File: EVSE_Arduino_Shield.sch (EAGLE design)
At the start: 45 parts, among them IC1 TLV1805DBVR, IC2 MT3608, IC3 TC1044S_OA, U2 ARDUINOR3-DIMENSION

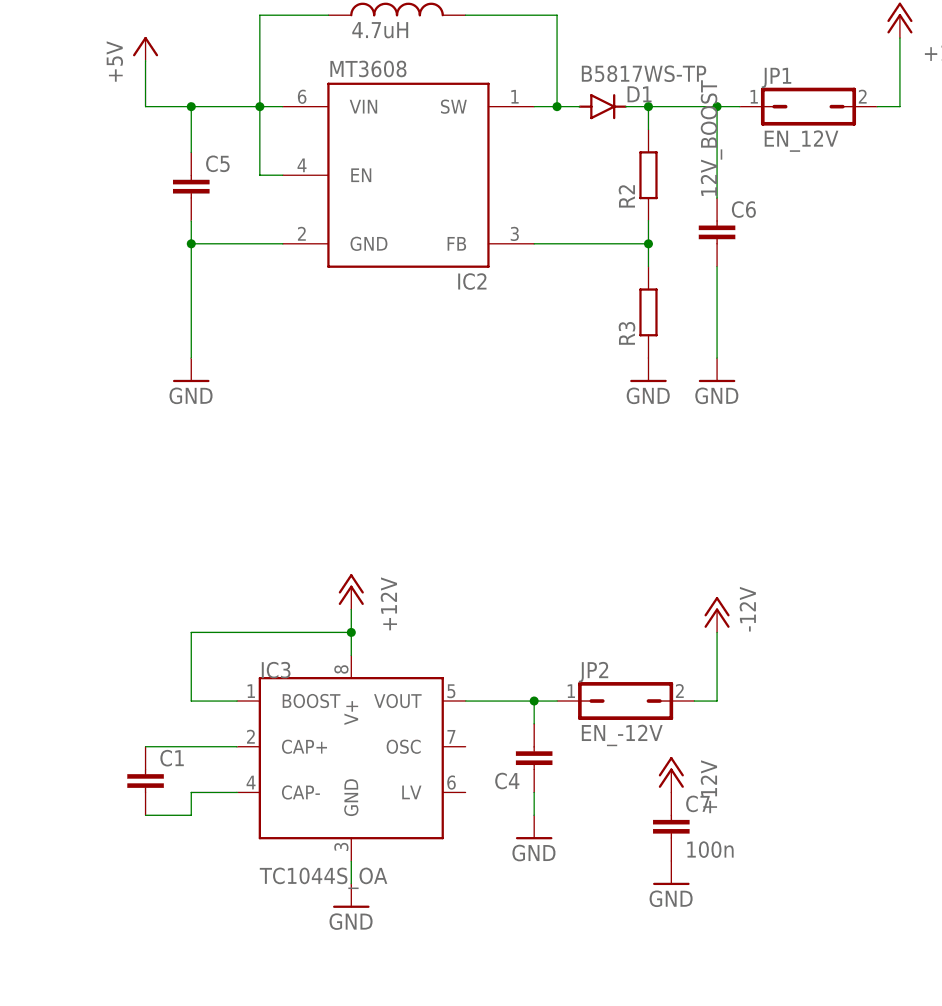
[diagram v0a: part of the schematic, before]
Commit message: * Fixed missing values of R2, R3, C5, C1, C6, C4
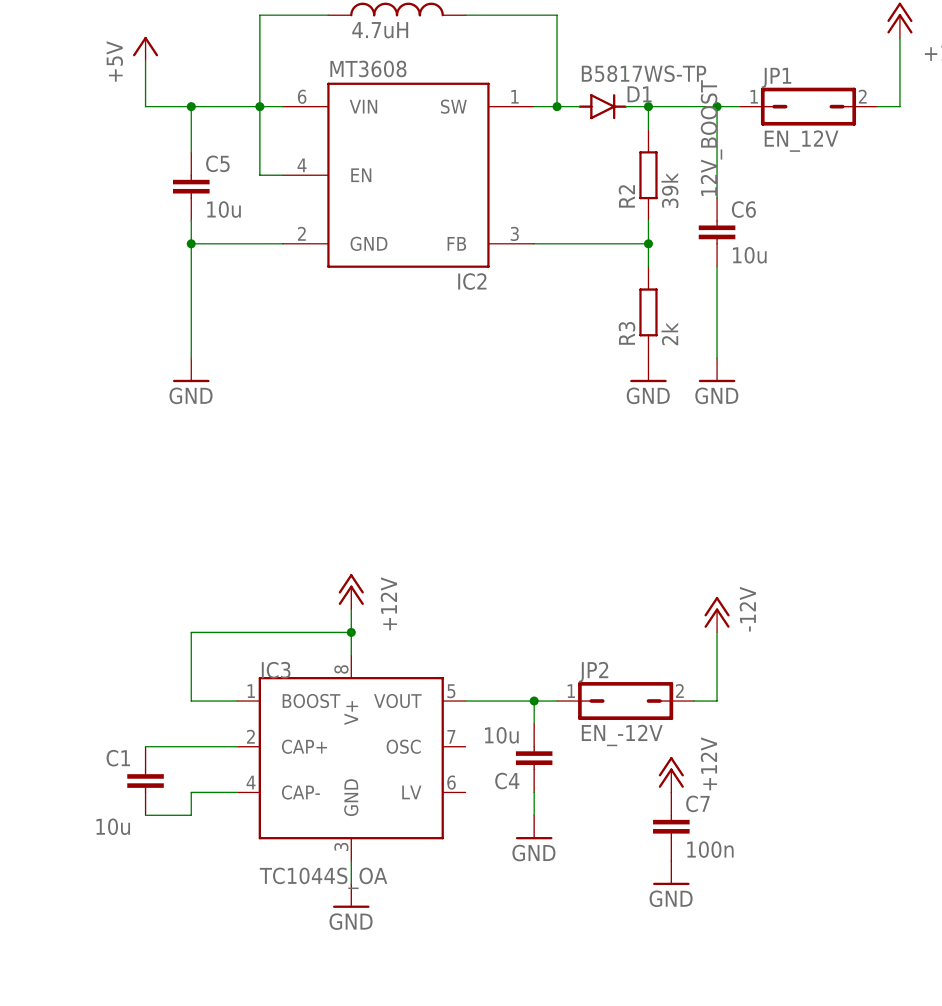
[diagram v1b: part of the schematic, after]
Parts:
- C1, C4, C5, C6: value (none) -> 10u
- R2: value (none) -> 39k
- R3: value (none) -> 2k
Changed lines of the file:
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@@
 <part name="GND6" library="supply1" library_urn="urn:adsk.eagle:library:371" deviceset="GND" device=""/>
 <part name="P-1" library="supply1" library_urn="urn:adsk.eagle:library:371" deviceset="-12V" device=""/>
-<part name="C1" library="rcl" library_urn="urn:adsk.eagle:library:334" deviceset="C-EU" device="C0805" package3d_urn="urn:adsk.eagle:package:23617/2"/>
-<part name="C4" library="rcl" library_urn="urn:adsk.eagle:library:334" deviceset="C-EU" device="C0805" package3d_urn="urn:adsk.eagle:package:23617/2"/>
+<part name="C1" library="rcl" library_urn="urn:adsk.eagle:library:334" deviceset="C-EU" device="C0805" package3d_urn="urn:adsk.eagle:package:23617/2" value="10u"/>
+<part name="C4" library="rcl" library_urn="urn:adsk.eagle:library:334" deviceset="C-EU" device="C0805" package3d_urn="urn:adsk.eagle:package:23617/2" value="10u"/>
 <part name="SV1" library="con-lstb" library_urn="urn:adsk.eagle:library:162" deviceset="MA03-1" device="" package3d_urn="urn:adsk.eagle:package:8339/1" value="12V_Test"/>
 <part name="GND1" library="supply1" library_urn="urn:adsk.eagle:library:371" deviceset="GND" device=""/>
@@
 <part name="IC2" library="Eigene-Rietig" library_urn="urn:adsk.eagle:library:40964436" deviceset="MT3608" device="" package3d_urn="urn:adsk.eagle:package:41021867/1"/>
 <part name="D1" library="diode" library_urn="urn:adsk.eagle:library:210" deviceset="DIODE-" device="SOD323-R" package3d_urn="urn:adsk.eagle:package:43437/1" value="B5817WS-TP"/>
-<part name="R2" library="rcl" library_urn="urn:adsk.eagle:library:334" deviceset="R-EU_" device="R0603" package3d_urn="urn:adsk.eagle:package:23555/3"/>
-<part name="R3" library="rcl" library_urn="urn:adsk.eagle:library:334" deviceset="R-EU_" device="R0603" package3d_urn="urn:adsk.eagle:package:23555/3"/>
-<part name="C5" library="rcl" library_urn="urn:adsk.eagle:library:334" deviceset="C-EU" device="C0805" package3d_urn="urn:adsk.eagle:package:23617/2"/>
-<part name="C6" library="rcl" library_urn="urn:adsk.eagle:library:334" deviceset="C-EU" device="C0805" package3d_urn="urn:adsk.eagle:package:23617/2"/>
+<part name="R2" library="rcl" library_urn="urn:adsk.eagle:library:334" deviceset="R-EU_" device="R0603" package3d_urn="urn:adsk.eagle:package:23555/3" value="39k"/>
+<part name="R3" library="rcl" library_urn="urn:adsk.eagle:library:334" deviceset="R-EU_" device="R0603" package3d_urn="urn:adsk.eagle:package:23555/3" value="2k"/>
+<part name="C5" library="rcl" library_urn="urn:adsk.eagle:library:334" deviceset="C-EU" device="C0805" package3d_urn="urn:adsk.eagle:package:23617/2" value="10u"/>
+<part name="C6" library="rcl" library_urn="urn:adsk.eagle:library:334" deviceset="C-EU" device="C0805" package3d_urn="urn:adsk.eagle:package:23617/2" value="10u"/>
 <part name="P+3" library="supply1" deviceset="+12V" device=""/>
 <part name="GND7" library="supply1" library_urn="urn:adsk.eagle:library:371" deviceset="GND" device=""/>
@@
 </instance>
 <instance part="C1" gate="G$1" x="30.48" y="137.16" smashed="yes">
-<attribute name="NAME" x="32.004" y="137.541" size="1.778" layer="95"/>
-<attribute name="VALUE" x="32.004" y="132.461" size="1.778" layer="96"/>
+<attribute name="NAME" x="28.956" y="139.319" size="1.778" layer="95" rot="R180"/>
+<attribute name="VALUE" x="28.956" y="131.699" size="1.778" layer="96" rot="R180"/>
 </instance>
 <instance part="C4" gate="G$1" x="73.66" y="137.16" smashed="yes" rot="R180">
@@
 </instance>
 <instance part="P+8" gate="1" x="88.9" y="137.16" smashed="yes">
-<attribute name="VALUE" x="93.98" y="132.08" size="1.778" layer="96" rot="R90"/>
+<attribute name="VALUE" x="93.98" y="134.62" size="1.778" layer="96" rot="R90"/>
 </instance>
 <instance part="C7" gate="G$1" x="88.9" y="132.08" smashed="yes">

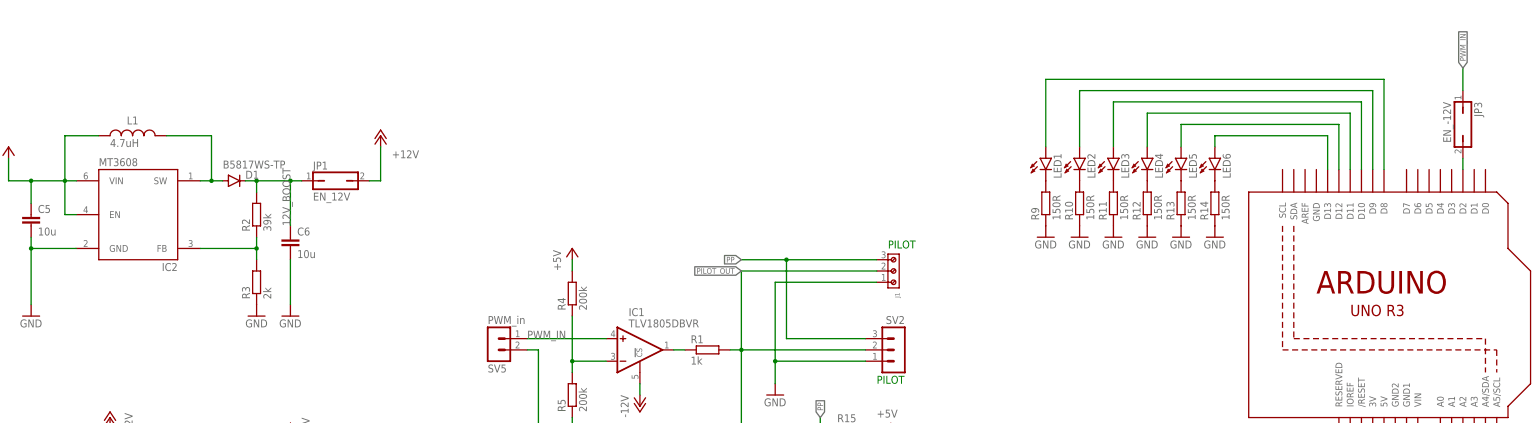
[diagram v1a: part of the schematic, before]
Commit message: * Cleaned Code a bit * Fixed Issue #1 - PWM is now on D3 * Fixed Issue #2 . MT3608 has the correct pin out now * Re-generated GERBER and SCH
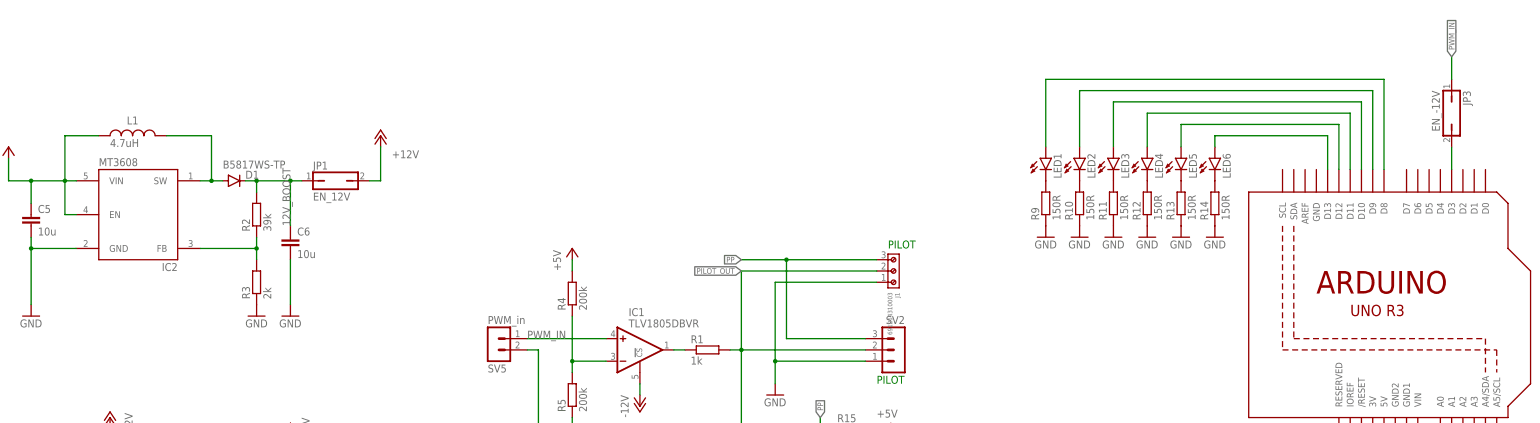
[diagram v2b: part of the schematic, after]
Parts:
- J1: value (none) -> 691214310003
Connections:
- net N$5: now also U2.D3; no longer U2.D2
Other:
- moved on the sheet: JP3
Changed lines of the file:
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@@
 <attribute name="NAME" x="232.41" y="131.318" size="1.778" layer="95" rot="R180"/>
 </instance>
-<instance part="JP3" gate="A" x="358.14" y="223.52" smashed="yes" rot="R180">
-<attribute name="NAME" x="360.68" y="228.6" size="1.778" layer="95" rot="R270"/>
-<attribute name="VALUE" x="353.695" y="228.6" size="1.778" layer="96" rot="R270"/>
+<instance part="JP3" gate="A" x="355.6" y="226.06" smashed="yes" rot="R180">
+<attribute name="NAME" x="358.14" y="231.14" size="1.778" layer="95" rot="R270"/>
+<attribute name="VALUE" x="351.155" y="231.14" size="1.778" layer="96" rot="R270"/>
 </instance>
 </instances>
@@
 </segment>
 <segment>
-<wire x1="358.14" y1="231.14" x2="358.14" y2="236.22" width="0.1524" layer="91"/>
-<label x="358.14" y="236.22" size="1.27" layer="95" rot="R90" xref="yes"/>
+<wire x1="355.6" y1="233.68" x2="355.6" y2="238.76" width="0.1524" layer="91"/>
+<label x="355.6" y="238.76" size="1.27" layer="95" rot="R90" xref="yes"/>
 <pinref part="JP3" gate="A" pin="1"/>
 </segment>
@@
 <net name="N$5" class="0">
 <segment>
-<pinref part="U2" gate="G$1" pin="D2"/>
 <pinref part="JP3" gate="A" pin="2"/>
-<wire x1="358.14" y1="213.36" x2="358.14" y2="215.9" width="0.1524" layer="91"/>
-</segment>
-</net>
+<pinref part="U2" gate="G$1" pin="D3"/>
+<wire x1="355.6" y1="213.36" x2="355.6" y2="218.44" width="0.1524" layer="91"/>
+</segment>
+</net>
